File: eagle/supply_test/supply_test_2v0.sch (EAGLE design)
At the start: 29 parts, among them J21 AC_INFILM, Q1 2N7002, U1 TPS62122

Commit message: placement done
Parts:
- added TP5: TP_STD, skyspecs:TP_STD
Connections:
- net PS_!EN!: now also TP5.P$1
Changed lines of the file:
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@@
 </part>
 <part name="TP4" library="skyspecs" deviceset="TP" device="_STD"/>
+<part name="TP5" library="skyspecs" deviceset="TP" device="_STD"/>
 </parts>
 <sheets>
@@
 <instance part="GND7" gate="1" x="63.5" y="-30.48"/>
 <instance part="TP4" gate="G$1" x="50.8" y="10.16"/>
+<instance part="TP5" gate="G$1" x="15.24" y="-40.64"/>
 </instances>
 <busses>
@@
 <label x="-43.18" y="-17.78" size="1.27" layer="95" rot="R180" xref="yes"/>
 </segment>
-</net>
+<segment>
+<pinref part="TP5" gate="G$1" pin="P$1"/>
+<wire x1="7.62" y1="-40.64" x2="10.16" y2="-40.64" width="0.1524" layer="91"/>
+<label x="7.62" y="-40.64" size="1.27" layer="95" rot="R180" xref="yes"/>
+</segment>
+</net>

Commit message: added pot to supply test
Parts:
- added C14, C2: 0.1uF, rcl:C-EUC0603
- added C15: 10uF, rcl:C-EUC0603
- added C16: 470nF, rcl:C-EUC0603
- added J1: JTAG_14PIN_IDC-NL, ibat:JTAG_14PIN_IDC-NL
- added R12: 660, rcl:R-US_R0603
- added R19: 47k, rcl:R-US_R0603
- added U$1: AD524, powerfilm:AD524
- added U4: MSP430FR5738, powerfilm:MSP430FR5738
- R11: value 4.99k -> 47k
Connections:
- new net N$12: R12.2, U$1.B
- new net N$23: C16.2, U4.VCORE
- new net RST: J1.11, R19.1, U4.RST
- new net SCL: U$1.SCL, U4.P1.7/TA1.0/UCBSCL/MISO
- new net SDA: U$1.SDA, U4.P1.6/TA0.0/UCBSDA/MOSI
- new net TCK: J1.7, U4.TCK
- new net TDI: J1.3, U4.TDI
- new net TDO: J1.1, U4.TDO
- new net TEST: J1.8, U4.TEST
- new net TMS: J1.5, U4.TMS
- net +3V3: now also C14.1, C15.1, C2.1, J1.2, R19.2, U$1.VDD, U$1.W, U4.AVCC, U4.DVCC
- net GND: now also C14.2, C15.2, C16.1, C2.2, J1.9, R12.1, U$1.AD0, U$1.GND, U4.AVSS, U4.DVSS

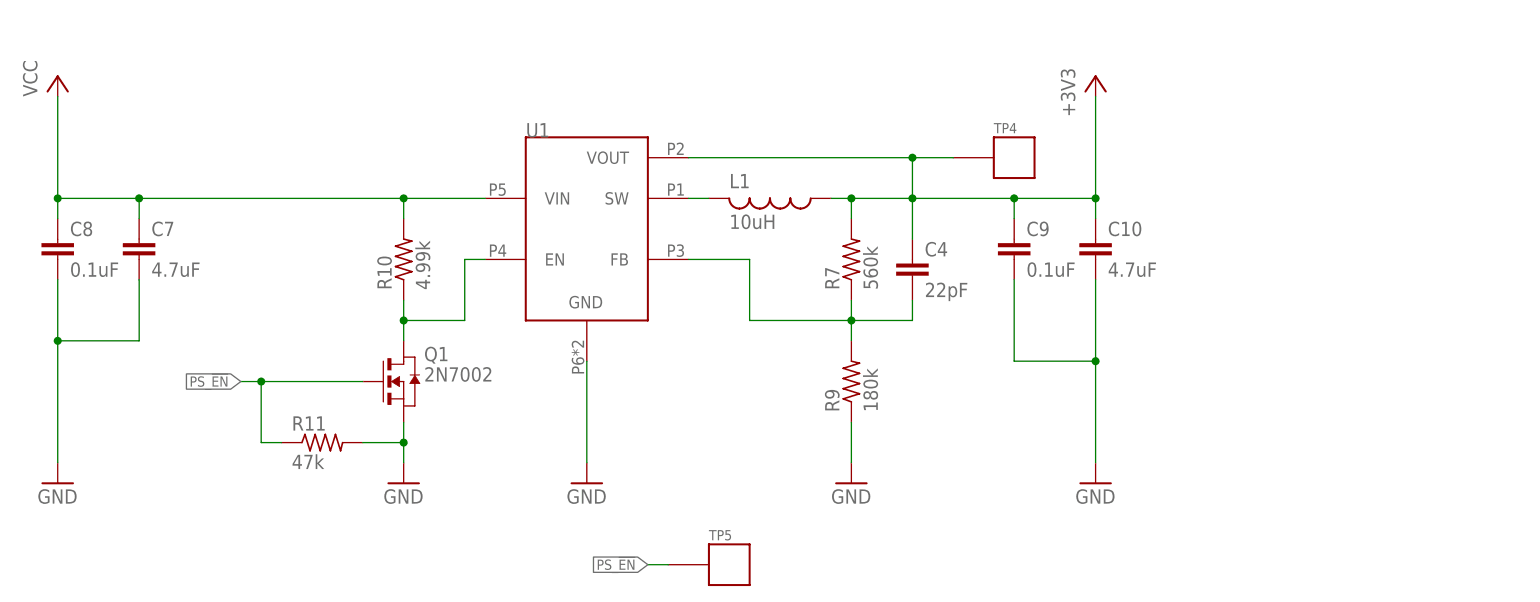
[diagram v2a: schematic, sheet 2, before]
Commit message: finished routing in new features
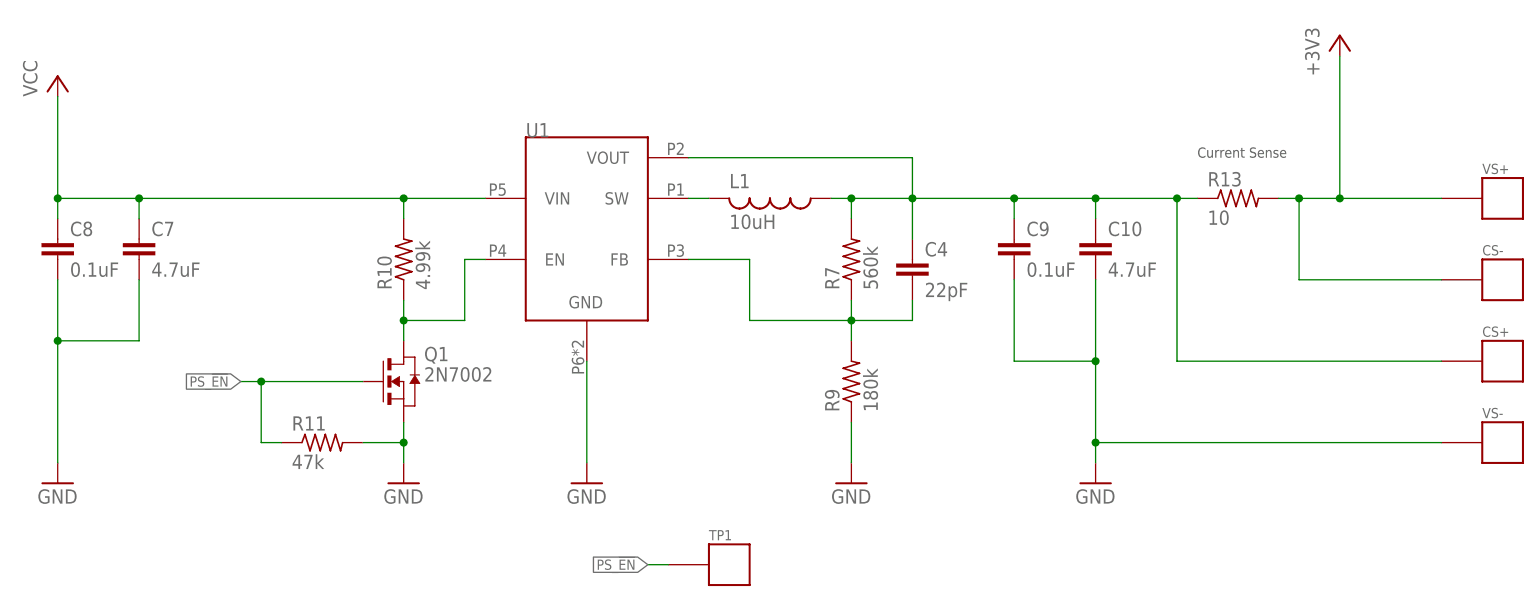
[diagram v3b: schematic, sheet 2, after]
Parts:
- removed TP4, TP5: TP_STD, skyspecs:TP_STD
- added CS+, CS-, RS+, VS+, VS-: TP_STD, skyspecs:TP_STD
- added R13: 10, rcl:R-US_R0603
- C9: device rcl:C-EUC0603 -> rcl:C-EUC0402
- TP1: DIGIKEY 5000K-ND -> (none)
- renumbered TP2 to RS-, TP3 to HVS
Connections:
- new net N$11: C10.1, C4.1, C9.1, CS+.P$1, L1.1, R13.1, R7.2, U1.VOUT
- net +3V3: now also CS-.P$1, R13.2, VS+.P$1; no longer C10.1, C4.1, C9.1, L1.1, R7.2, TP4.P$1, U1.VOUT
- net GND: now also VS-.P$1
- net PS_!EN!: now also TP1.P$1; no longer TP5.P$1
- net VCC: now also RS+.P$1; no longer TP1.P$1
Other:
- note added: "Current Sense"

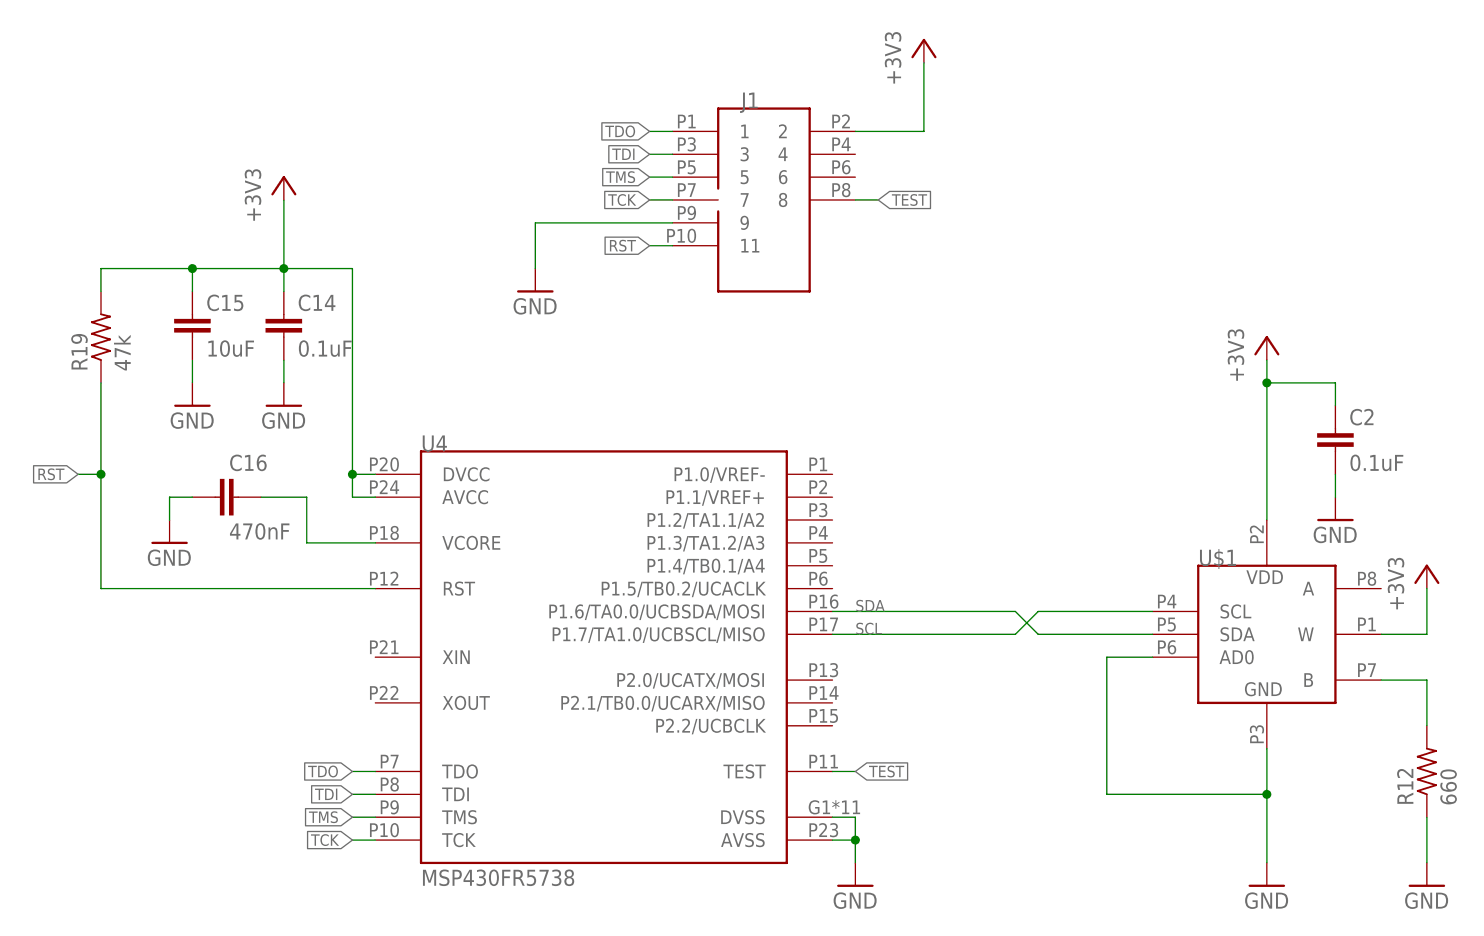
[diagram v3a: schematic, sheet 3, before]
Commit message: all parts numbered in supply test v2
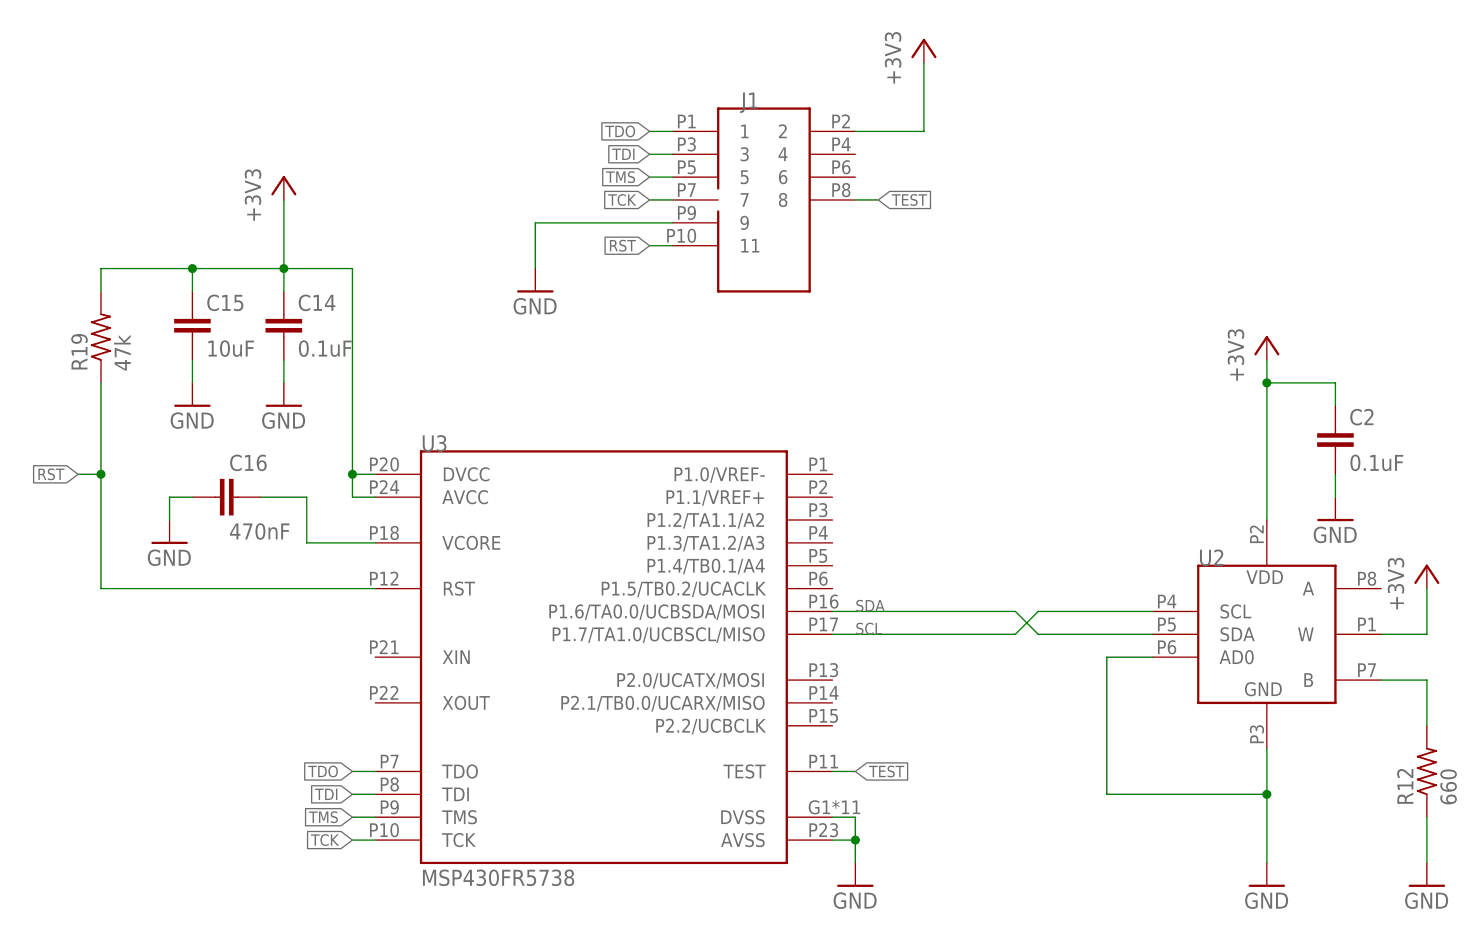
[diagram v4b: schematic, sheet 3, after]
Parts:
- C10, C7: DIGIKEY (none) -> 587-2786-1-ND
- C3: value (none) -> 33uF
- C4: DIGIKEY (none) -> 399-1053-1-ND
- C8, C9: DIGIKEY (none) -> 1276-1001-1-ND
- CS+, CS-, R4, R5, R6, TP1, VS+, VS-: DIGIKEY (none) -> NP
- D1: DIGIKEY (none) -> BZT52C10T-7DICT-ND; DIGIKEY_2 BZT585B5V1T-7DICT-ND -> BZT52C15T-7DICT-ND; DIGIKEY_3 BZT585B6V8T-7DICT-ND -> (none)
- J21: DIGIKEY (none) -> NP; DIGIKEY_2 AE9888-ND -> (none)
- R10: value 4.99k -> 10k; DIGIKEY (none) -> P10KJCT-ND
- R11: DIGIKEY (none) -> P47KGCT-ND
- R12: DIGIKEY (none) -> P665HCT-ND
- R2, R3: DIGIKEY (none) -> P0.0GCT-ND
- R7: DIGIKEY (none) -> P560KHCT-ND
- R9: DIGIKEY (none) -> P180KHCT-ND
- RS+: DIGIKEY 5000K-ND -> NP
- RS-: DIGIKEY 5001K-ND -> NP
- renumbered U$1 to U2, U4 to U3
